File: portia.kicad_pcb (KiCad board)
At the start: 2 copper layers, 42.3 x 30.6 mm, 7 parts, among them SW1 Reset, SW2 Reset, U4 ESP32-WROOM

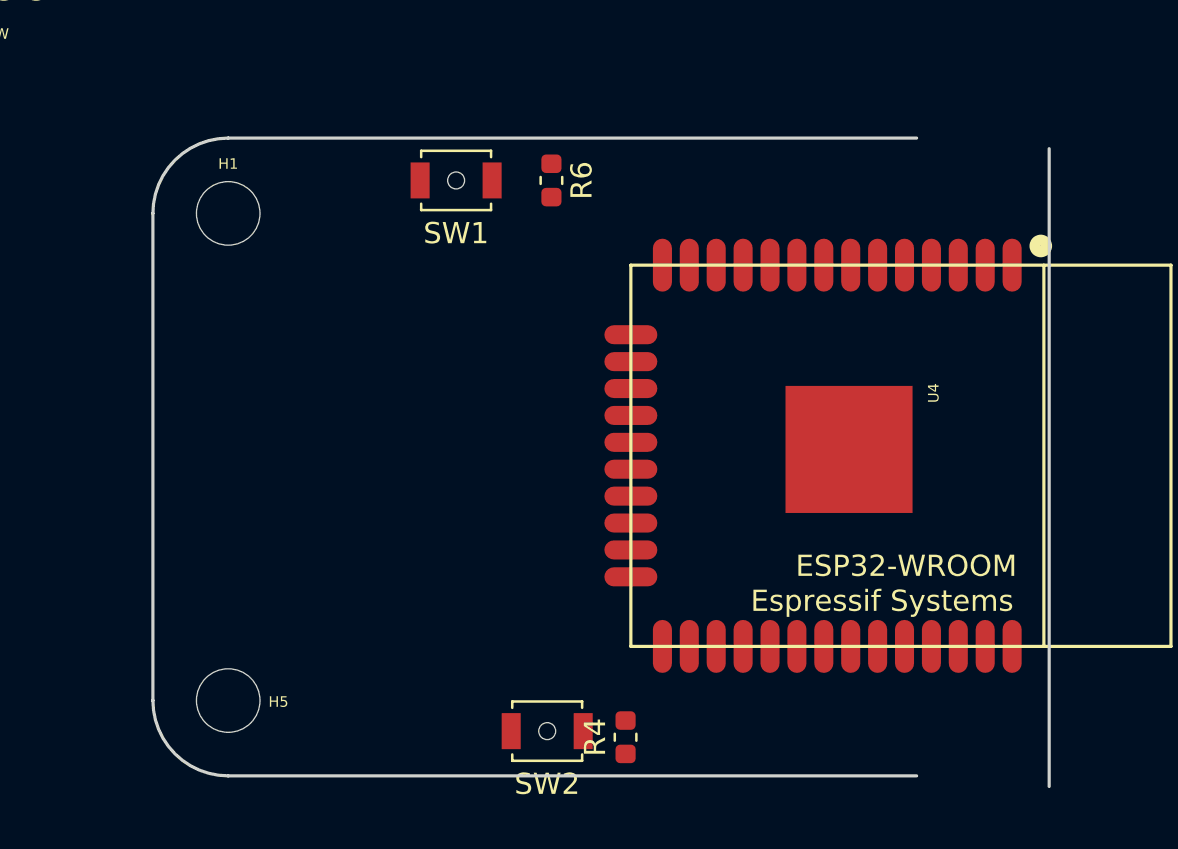
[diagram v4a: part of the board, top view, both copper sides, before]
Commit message: add castellated footprint
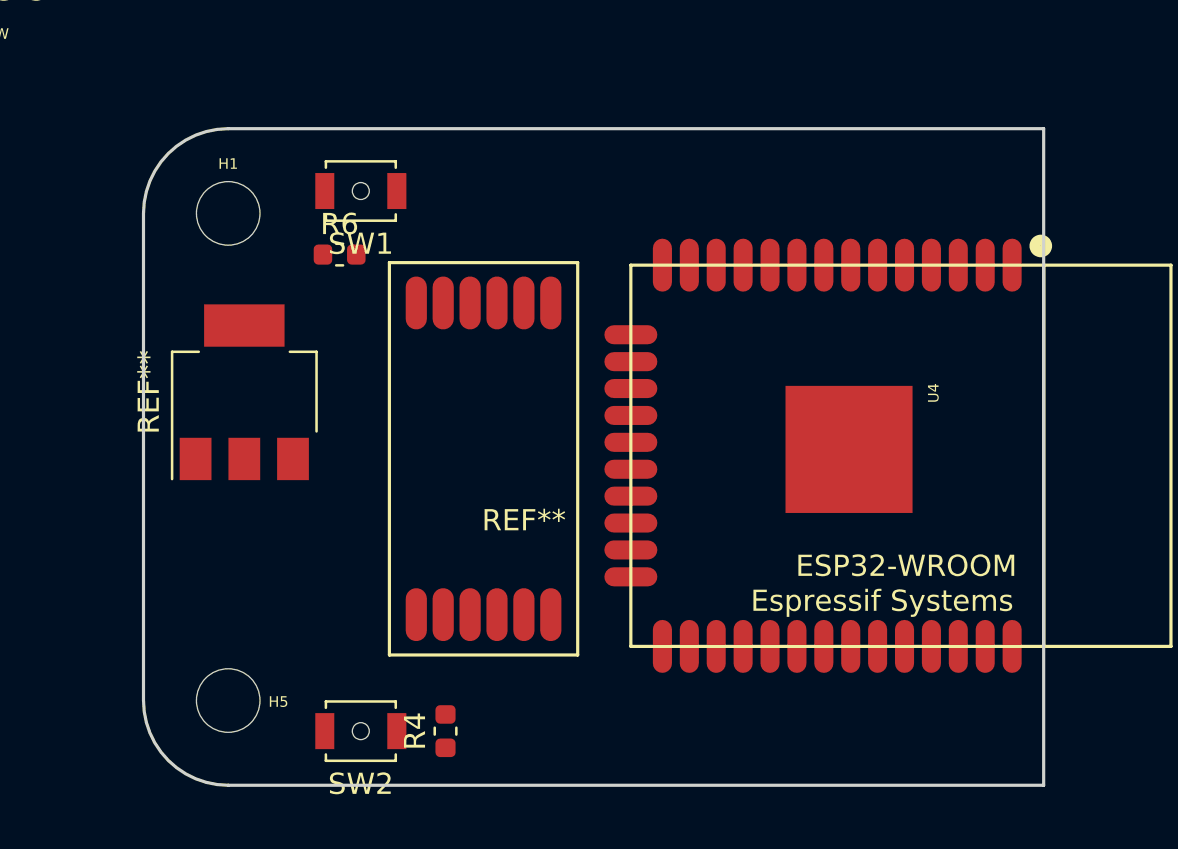
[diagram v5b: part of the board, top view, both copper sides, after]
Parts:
- added REF**: castellated12, sb_designed_footprints:castellated12, F.Cu at (176.5, 117.2)
- added REF**: SOT-223-3_TabPin2, Package_TO_SOT_SMD:SOT-223-3_TabPin2, F.Cu at (160.8, 115.7)
- moved R6 10.6 mm to (165.3, 109.2), turned to 0 degrees
- moved SW2 8.80 mm to (166.3, 131.7)
- moved R4 8.50 mm to (170.3, 131.7)
- moved SW1 4.53 mm to (166.3, 106.2)
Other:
- board size 42.3 x 30.6 mm -> 42.5 x 31 mm
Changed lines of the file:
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@@
     (tracks 0)
     (zones 0)
-    (modules 7)
+    (modules 9)
     (nets 37)
   )
@@
     (solder_mask_min_width 0.25)
     (aux_axis_origin 167.22 97.514)
-    (grid_origin 175.78 109.724)
+    (grid_origin 160.02 107.28)
     (visible_elements FFFFF77F)
     (pcbplotparams
@@
     (uvia_dia 0.3)
     (uvia_drill 0.1)
+  )
+  (module sb_designed_footprints:castellated12 (layer F.Cu)
+    (at 176.52 117.224)
+    (fp_text reference REF** (at -2.54 4.555) (layer F.SilkS)
+      (effects (font (size 1 1) (thickness 0.15)))
+    )
+    (fp_text value castellated12 (at -7.62 1.905 90) (layer F.Fab)
+      (effects (font (size 1 1) (thickness 0.15)))
+    )
+    (fp_line (start -8.89 -7.62) (end 0 -7.62) (layer F.SilkS) (width 0.15))
+    (fp_line (start 0 -7.62) (end 0 10.905) (layer F.SilkS) (width 0.15))
+    (fp_line (start 0 10.905) (end -8.89 10.905) (layer F.SilkS) (width 0.15))
+    (fp_line (start -8.89 10.905) (end -8.89 -7.62) (layer F.SilkS) (width 0.15))
+    (pad 1 smd oval (at -7.62 -5.715) (size 1 2.5) (layers F.Cu F.Paste F.Mask))
+    (pad 2 smd oval (at -6.35 -5.715) (size 1 2.5) (layers F.Cu F.Paste F.Mask))
+    (pad 3 smd oval (at -5.08 -5.715) (size 1 2.5) (layers F.Cu F.Paste F.Mask))
+    (pad 4 smd oval (at -3.81 -5.715) (size 1 2.5) (layers F.Cu F.Paste F.Mask))
+    (pad 6 smd oval (at -2.54 -5.715) (size 1 2.5) (layers F.Cu F.Paste F.Mask))
+    (pad 5 smd oval (at -1.27 -5.715) (size 1 2.5) (layers F.Cu F.Paste F.Mask))
+    (pad 7 smd oval (at -7.62 9) (size 1 2.5) (layers F.Cu F.Paste F.Mask))
+    (pad 9 smd oval (at -6.35 9) (size 1 2.5) (layers F.Cu F.Paste F.Mask))
+    (pad 8 smd oval (at -5.08 9) (size 1 2.5) (layers F.Cu F.Paste F.Mask))
+    (pad 10 smd oval (at -3.81 9) (size 1 2.5) (layers F.Cu F.Paste F.Mask))
+    (pad 11 smd oval (at -2.54 9) (size 1 2.5) (layers F.Cu F.Paste F.Mask))
+    (pad 12 smd oval (at -1.27 9) (size 1 2.5) (layers F.Cu F.Paste F.Mask))
   )
   (module ESP32-footprints-Lib:ESP32-WROOM (layer F.Cu)
@@
   )
   (module Resistor_SMD:R_0603_1608Metric (layer F.Cu)
-    (at 175.28 105.724 270)
+    (at 165.28 109.224)
     (descr "Resistor SMD 0603 (1608 Metric), square (rectangular) end terminal, IPC_7351 nominal, (Body size source: http://www.tortai-tech.com/upload/download/2011102023233369053.pdf), generated with kicad-footprint-generator")
     (tags resistor)
     (attr smd)
-    (fp_text reference R6 (at 0 -1.43 270) (layer F.SilkS)
-      (effects (font (size 1 1) (thickness 0.15)))
-    )
-    (fp_text value R10K (at 0 1.43 270) (layer F.Fab)
-      (effects (font (size 1 1) (thickness 0.15)))
-    )
-    (fp_text user %R (at 0 0 270) (layer F.Fab)
+    (fp_text reference R6 (at 0 -1.43) (layer F.SilkS)
+      (effects (font (size 1 1) (thickness 0.15)))
+    )
+    (fp_text value R10K (at 0 1.43) (layer F.Fab)
+      (effects (font (size 1 1) (thickness 0.15)))
+    )
+    (fp_text user %R (at 0 0) (layer F.Fab)
       (effects (font (size 0.4 0.4) (thickness 0.06)))
     )
@@
     (fp_line (start -0.8 -0.4) (end 0.8 -0.4) (layer F.Fab) (width 0.1))
     (fp_line (start -0.8 0.4) (end -0.8 -0.4) (layer F.Fab) (width 0.1))
-    (pad 2 smd roundrect (at 0.7875 0 270) (size 0.875 0.95) (layers F.Cu F.Paste F.Mask) (roundrect_rratio 0.25)
+    (pad 2 smd roundrect (at 0.7875 0) (size 0.875 0.95) (layers F.Cu F.Paste F.Mask) (roundrect_rratio 0.25)
       (net 1 +3V3))
-    (pad 1 smd roundrect (at -0.7875 0 270) (size 0.875 0.95) (layers F.Cu F.Paste F.Mask) (roundrect_rratio 0.25)
+    (pad 1 smd roundrect (at -0.7875 0) (size 0.875 0.95) (layers F.Cu F.Paste F.Mask) (roundrect_rratio 0.25)
       (net 14 "Net-(R6-Pad1)"))
     (model ${KISYS3DMOD}/Resistor_SMD.3dshapes/R_0603_1608Metric.wrl
@@
   )
   (module Button_Switch_SMD:SW_SPST_B3U-1000P-B (layer F.Cu)
-    (at 175.08 131.724 180)
+    (at 166.28 131.724 180)
     (descr "Ultra-small-sized Tactile Switch with High Contact Reliability, Top-actuated Model, without Ground Terminal, with Boss")
     (tags "Tactile Switch")
@@
   )
   (module Button_Switch_SMD:SW_SPST_B3U-1000P-B (layer F.Cu)
-    (at 170.78 105.724 180)
+    (at 166.28 106.224 180)
     (descr "Ultra-small-sized Tactile Switch with High Contact Reliability, Top-actuated Model, without Ground Terminal, with Boss")
     (tags "Tactile Switch")
@@
   )
   (module Resistor_SMD:R_0603_1608Metric (layer F.Cu)
-    (at 178.78 132.0115 90)
+    (at 170.28 131.724 90)
     (descr "Resistor SMD 0603 (1608 Metric), square (rectangular) end terminal, IPC_7351 nominal, (Body size source: http://www.tortai-tech.com/upload/download/2011102023233369053.pdf), generated with kicad-footprint-generator")
     (tags resistor)
@@
     (pad 1 np_thru_hole circle (at 0 0) (size 3 3) (drill 3) (layers *.Cu *.Mask))
   )
-  (gr_line (start 156.464 130.28) (end 156.464 107.28) (layer Edge.Cuts) (width 0.15))
-  (gr_line (start 160.02 103.724) (end 192.52 103.724) (layer Edge.Cuts) (width 0.15))
-  (gr_line (start 198.78 134.336) (end 198.78 104.224) (layer Edge.Cuts) (width 0.15))
-  (gr_line (start 160.02 133.836) (end 192.52 133.836) (layer Edge.Cuts) (width 0.15))
+  (module Package_TO_SOT_SMD:SOT-223-3_TabPin2 (layer F.Cu)
+    (at 160.78 115.724 90)
+    (descr "module CMS SOT223 4 pins")
+    (tags "CMS SOT")
+    (attr smd)
+    (fp_text reference REF** (at 0 -4.5 90) (layer F.SilkS)
+      (effects (font (size 1 1) (thickness 0.15)))
+    )
+    (fp_text value SOT-223-3_TabPin2 (at 0 4.5 90) (layer F.Fab)
+      (effects (font (size 1 1) (thickness 0.15)))
+    )
+    (fp_line (start 1.85 -3.35) (end 1.85 3.35) (layer F.Fab) (width 0.1))
+    (fp_line (start -1.85 3.35) (end 1.85 3.35) (layer F.Fab) (width 0.1))
+    (fp_line (start -4.1 -3.41) (end 1.91 -3.41) (layer F.SilkS) (width 0.12))
+    (fp_line (start -0.85 -3.35) (end 1.85 -3.35) (layer F.Fab) (width 0.1))
+    (fp_line (start -1.85 3.41) (end 1.91 3.41) (layer F.SilkS) (width 0.12))
+    (fp_line (start -1.85 -2.35) (end -1.85 3.35) (layer F.Fab) (width 0.1))
+    (fp_line (start -1.85 -2.35) (end -0.85 -3.35) (layer F.Fab) (width 0.1))
+    (fp_line (start -4.4 -3.6) (end -4.4 3.6) (layer F.CrtYd) (width 0.05))
+    (fp_line (start -4.4 3.6) (end 4.4 3.6) (layer F.CrtYd) (width 0.05))
+    (fp_line (start 4.4 3.6) (end 4.4 -3.6) (layer F.CrtYd) (width 0.05))
+    (fp_line (start 4.4 -3.6) (end -4.4 -3.6) (layer F.CrtYd) (width 0.05))
+    (fp_line (start 1.91 -3.41) (end 1.91 -2.15) (layer F.SilkS) (width 0.12))
+    (fp_line (start 1.91 3.41) (end 1.91 2.15) (layer F.SilkS) (width 0.12))
+    (fp_text user %R (at 0 0 180) (layer F.Fab)
+      (effects (font (size 0.8 0.8) (thickness 0.12)))
+    )
+    (pad 1 smd rect (at -3.15 -2.3 90) (size 2 1.5) (layers F.Cu F.Paste F.Mask))
+    (pad 3 smd rect (at -3.15 2.3 90) (size 2 1.5) (layers F.Cu F.Paste F.Mask))
+    (pad 2 smd rect (at -3.15 0 90) (size 2 1.5) (layers F.Cu F.Paste F.Mask))
+    (pad 2 smd rect (at 3.15 0 90) (size 2 3.8) (layers F.Cu F.Paste F.Mask))
+    (model ${KISYS3DMOD}/Package_TO_SOT_SMD.3dshapes/SOT-223.wrl
+      (at (xyz 0 0 0))
+      (scale (xyz 1 1 1))
+      (rotate (xyz 0 0 0))
+    )
+  )
+  (gr_line (start 160.02 103.28) (end 198.52 103.28) (layer Edge.Cuts) (width 0.15))
+  (gr_line (start 198.52 103.28) (end 198.52 134.28) (layer Edge.Cuts) (width 0.15))
+  (gr_line (start 156.02 107.28) (end 156.02 130.28) (layer Edge.Cuts) (width 0.15))
+  (gr_arc (start 160.02 130.28) (end 156.02 130.28) (angle -90) (layer Edge.Cuts) (width 0.15))
+  (gr_arc (start 160.02 107.28) (end 160.02 103.28) (angle -90) (layer Edge.Cuts) (width 0.15))
+  (gr_line (start 160.02 134.28) (end 198.52 134.28) (layer Edge.Cuts) (width 0.15))
   (gr_circle (center 148.156 96.514) (end 148.156 96.768) (layer F.SilkS) (width 0.2))
   (gr_circle (center 152.22 96.514) (end 152.22 96.768) (layer F.SilkS) (width 0.2))
@@
     (effects (font (size 1.5 1.5) (thickness 0.125)))
   )
-  (gr_arc (start 160.02 130.28) (end 156.464 130.28) (angle -90) (layer Edge.Cuts) (width 0.15))
-  (gr_arc (start 160.02 107.28) (end 160.02 103.724) (angle -90) (layer Edge.Cuts) (width 0.15))
 )

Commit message: update layout
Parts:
- removed REF**: castellated12, sb_designed_footprints:castellated12
- removed REF**: SOT-223-3_TabPin2, Package_TO_SOT_SMD:SOT-223-3_TabPin2
- added C1: C_Small, Capacitor_SMD:C_0603_1608Metric_Pad1.05x0.95mm_HandSolder, F.Cu at (158.8, 124.1)
- added C2: C_Small, Capacitor_SMD:C_0603_1608Metric_Pad1.05x0.95mm_HandSolder, F.Cu at (162.5, 121.8)
- added J1: Conn_01x11, Connector_PinHeader_2.54mm:PinHeader_1x11_P2.54mm_Vertical, F.Cu at (170.9, 105.5)
- added J2: Conn_01x11, Connector_PinHeader_2.54mm:PinHeader_1x11_P2.54mm_Vertical, F.Cu at (196.3, 132.0)
- added J4: Conn_02x06_Odd_Even, sb_designed_footprints:castellated12, F.Cu at (168.0, 120.3)
- added U1: LM1117-3.3, Package_TO_SOT_SMD:SOT-223, F.Cu at (160.5, 115.8)
- moved R4 6.04 mm to (165.0, 128.8), turned to 0 degrees
- moved R6 0.30 mm to (165.0, 109.1), turned to 180 degrees

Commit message: add traces
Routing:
- net Net-(J1-Pad1): track 0.00 -> 17.0 mm
- net Net-(J1-Pad2): track 0.00 -> 14.8 mm
- net Net-(J1-Pad3): track 0.00 -> 14.3 mm, vias 0 -> 1
- net Net-(J1-Pad4): track 0.00 -> 13.0 mm, vias 0 -> 1
- net Net-(J2-Pad6): track 0.00 -> 12.3 mm
- net Net-(J1-Pad5): track 0.00 -> 11.8 mm, vias 0 -> 1
- net Net-(J2-Pad5): track 0.00 -> 11.3 mm
- net Net-(J1-Pad6): track 0.00 -> 10.4 mm
- net Net-(J2-Pad4): track 0.00 -> 10.3 mm
- net Net-(J1-Pad7): track 0.00 -> 9.62 mm
- net Net-(J1-Pad8): track 0.00 -> 7.19 mm
- net Net-(R6-Pad1): track 0.00 -> 2.00 mm, vias 0 -> 1
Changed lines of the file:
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@@
     (thickness 1.6)
     (drawings 13)
-    (tracks 0)
+    (tracks 70)
     (zones 0)
     (modules 13)
@@
     (solder_mask_min_width 0.25)
     (aux_axis_origin 167.22 97.514)
-    (grid_origin 196.27 132.03)
+    (grid_origin 194.49 109.724)
     (visible_elements FFFFF77F)
     (pcbplotparams
@@
     (effects (font (size 1.5 1.5) (thickness 0.125)))
   )
+  (segment (start 194.49 109.724) (end 194.49 107.724) (width 0.25) (layer F.Cu) (net 11))
+  (segment (start 194.49 107.724) (end 194.49 107.724) (width 0.25) (layer F.Cu) (net 11))
+  (via (at 194.49 107.724) (size 0.6) (drill 0.4) (layers F.Cu B.Cu) (net 11))
+  (segment (start 193.99 130.224) (end 187.916 130.224) (width 0.25) (layer F.Cu) (net 15))
+  (segment (start 194.49 129.724) (end 193.99 130.224) (width 0.25) (layer F.Cu) (net 15))
+  (segment (start 194.49 127.724) (end 194.49 129.724) (width 0.25) (layer F.Cu) (net 15))
+  (segment (start 187.916 130.224) (end 186.959999 131.180001) (width 0.25) (layer F.Cu) (net 15))
+  (segment (start 186.959999 131.180001) (end 186.11 132.03) (width 0.25) (layer F.Cu) (net 15))
+  (segment (start 191.95 109.724) (end 191.95 108.924) (width 0.25) (layer F.Cu) (net 16))
+  (segment (start 191.95 107.59641) (end 191.95 109.724) (width 0.25) (layer F.Cu) (net 16))
+  (segment (start 186.11 105.53) (end 187.36 106.78) (width 0.25) (layer F.Cu) (net 16))
+  (segment (start 187.36 106.78) (end 189.872412 106.78) (width 0.25) (layer F.Cu) (net 16))
+  (segment (start 189.872412 106.78) (end 190.372412 107.28) (width 0.25) (layer F.Cu) (net 16))
+  (segment (start 191.63359 107.28) (end 191.95 107.59641) (width 0.25) (layer F.Cu) (net 16))
+  (segment (start 190.372412 107.28) (end 191.63359 107.28) (width 0.25) (layer F.Cu) (net 16))
+  (segment (start 195.76 127.724) (end 195.76 130.204) (width 0.25) (layer F.Cu) (net 17))
+  (segment (start 195.76 130.204) (end 195.24 130.724) (width 0.25) (layer F.Cu) (net 17))
+  (segment (start 195.24 130.724) (end 189.956 130.724) (width 0.25) (layer F.Cu) (net 17))
+  (segment (start 189.956 130.724) (end 189.499999 131.180001) (width 0.25) (layer F.Cu) (net 17))
+  (segment (start 189.499999 131.180001) (end 188.65 132.03) (width 0.25) (layer F.Cu) (net 17))
+  (segment (start 184.419999 131.180001) (end 183.57 132.03) (width 0.25) (layer F.Cu) (net 18))
+  (segment (start 193.22 127.724) (end 193.22 129.244) (width 0.25) (layer F.Cu) (net 18))
+  (segment (start 193.22 129.244) (end 192.74 129.724) (width 0.25) (layer F.Cu) (net 18))
+  (segment (start 192.74 129.724) (end 185.876 129.724) (width 0.25) (layer F.Cu) (net 18))
+  (segment (start 185.876 129.724) (end 184.419999 131.180001) (width 0.25) (layer F.Cu) (net 18))
+  (segment (start 184.33 107.79001) (end 183.84001 107.30002) (width 0.25) (layer F.Cu) (net 21))
+  (segment (start 170.87 106.63) (end 170.87 105.53) (width 0.25) (layer F.Cu) (net 21))
+  (segment (start 184.33 109.724) (end 184.33 107.79001) (width 0.25) (layer F.Cu) (net 21))
+  (segment (start 171.54002 107.30002) (end 170.87 106.63) (width 0.25) (layer F.Cu) (net 21))
+  (segment (start 183.84001 107.30002) (end 171.54002 107.30002) (width 0.25) (layer F.Cu) (net 21))
+  (segment (start 185.6 108.224) (end 184.226009 106.850009) (width 0.25) (layer F.Cu) (net 22))
+  (segment (start 174.259999 106.379999) (end 173.41 105.53) (width 0.25) (layer F.Cu) (net 22))
+  (segment (start 185.6 109.724) (end 185.6 108.224) (width 0.25) (layer F.Cu) (net 22))
+  (segment (start 174.730009 106.850009) (end 174.259999 106.379999) (width 0.25) (layer F.Cu) (net 22))
+  (segment (start 184.226009 106.850009) (end 174.730009 106.850009) (width 0.25) (layer F.Cu) (net 22))
+  (segment (start 186.87 107.87001) (end 186.87 107.87001) (width 0.25) (layer F.Cu) (net 23))
+  (segment (start 186.87 109.724) (end 186.87 107.87001) (width 0.25) (layer F.Cu) (net 23))
+  (via (at 186.87 107.87001) (size 0.6) (drill 0.4) (layers F.Cu B.Cu) (net 23))
+  (segment (start 179.02001 108.60001) (end 175.95 105.53) (width 0.25) (layer B.Cu) (net 23))
+  (segment (start 186.14 108.60001) (end 179.02001 108.60001) (width 0.25) (layer B.Cu) (net 23))
+  (segment (start 186.87 107.87001) (end 186.14 108.60001) (width 0.25) (layer B.Cu) (net 23))
+  (segment (start 188.14 109.724) (end 188.14 107.85001) (width 0.25) (layer F.Cu) (net 24))
+  (segment (start 188.14 107.85001) (end 188.14 107.85001) (width 0.25) (layer F.Cu) (net 24))
+  (via (at 188.14 107.85001) (size 0.6) (drill 0.4) (layers F.Cu B.Cu) (net 24))
+  (segment (start 179.339999 106.379999) (end 178.49 105.53) (width 0.25) (layer B.Cu) (net 24))
+  (segment (start 180.81001 107.85001) (end 179.339999 106.379999) (width 0.25) (layer B.Cu) (net 24))
+  (segment (start 188.14 107.85001) (end 187.534999 107.245009) (width 0.25) (layer B.Cu) (net 24))
+  (segment (start 185.89 107.245009) (end 185.284999 107.85001) (width 0.25) (layer B.Cu) (net 24))
+  (segment (start 187.534999 107.245009) (end 185.89 107.245009) (width 0.25) (layer B.Cu) (net 24))
+  (segment (start 185.284999 107.85001) (end 180.81001 107.85001) (width 0.25) (layer B.Cu) (net 24))
+  (segment (start 189.41 109.724) (end 189.41 107.84001) (width 0.25) (layer F.Cu) (net 25))
+  (segment (start 189.41 107.84001) (end 189.41 107.84001) (width 0.25) (layer F.Cu) (net 25))
+  (via (at 189.41 107.84001) (size 0.6) (drill 0.4) (layers F.Cu B.Cu) (net 25))
+  (segment (start 181.879999 106.379999) (end 181.03 105.53) (width 0.25) (layer B.Cu) (net 25))
+  (segment (start 182.85001 107.35001) (end 181.879999 106.379999) (width 0.25) (layer B.Cu) (net 25))
+  (segment (start 189.41 107.84001) (end 188.274991 106.705001) (width 0.25) (layer B.Cu) (net 25))
+  (segment (start 185.39 106.705001) (end 184.744991 107.35001) (width 0.25) (layer B.Cu) (net 25))
+  (segment (start 188.274991 106.705001) (end 185.39 106.705001) (width 0.25) (layer B.Cu) (net 25))
+  (segment (start 184.744991 107.35001) (end 182.85001 107.35001) (width 0.25) (layer B.Cu) (net 25))
+  (segment (start 190.68 109.724) (end 190.68 109.097971) (width 0.25) (layer F.Cu) (net 26))
+  (segment (start 190.68 108.224) (end 189.736 107.28) (width 0.25) (layer F.Cu) (net 26))
+  (segment (start 184.419999 106.379999) (end 183.57 105.53) (width 0.25) (layer F.Cu) (net 26))
+  (segment (start 185.32 107.28) (end 184.419999 106.379999) (width 0.25) (layer F.Cu) (net 26))
+  (segment (start 190.68 109.724) (end 190.68 108.224) (width 0.25) (layer F.Cu) (net 26))
+  (segment (start 189.736 107.28) (end 185.32 107.28) (width 0.25) (layer F.Cu) (net 26))
+  (segment (start 193.22 108.224) (end 191.776 106.78) (width 0.25) (layer F.Cu) (net 27))
+  (segment (start 189.258822 105.53) (end 188.65 105.53) (width 0.25) (layer F.Cu) (net 27))
+  (segment (start 193.22 109.724) (end 193.22 108.224) (width 0.25) (layer F.Cu) (net 27))
+  (segment (start 191.776 106.78) (end 190.508822 106.78) (width 0.25) (layer F.Cu) (net 27))
+  (segment (start 190.508822 106.78) (end 189.258822 105.53) (width 0.25) (layer F.Cu) (net 27))
 )
